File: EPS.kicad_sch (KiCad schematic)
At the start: 42 parts, among them SW101 Deploy, SW102 Deploy

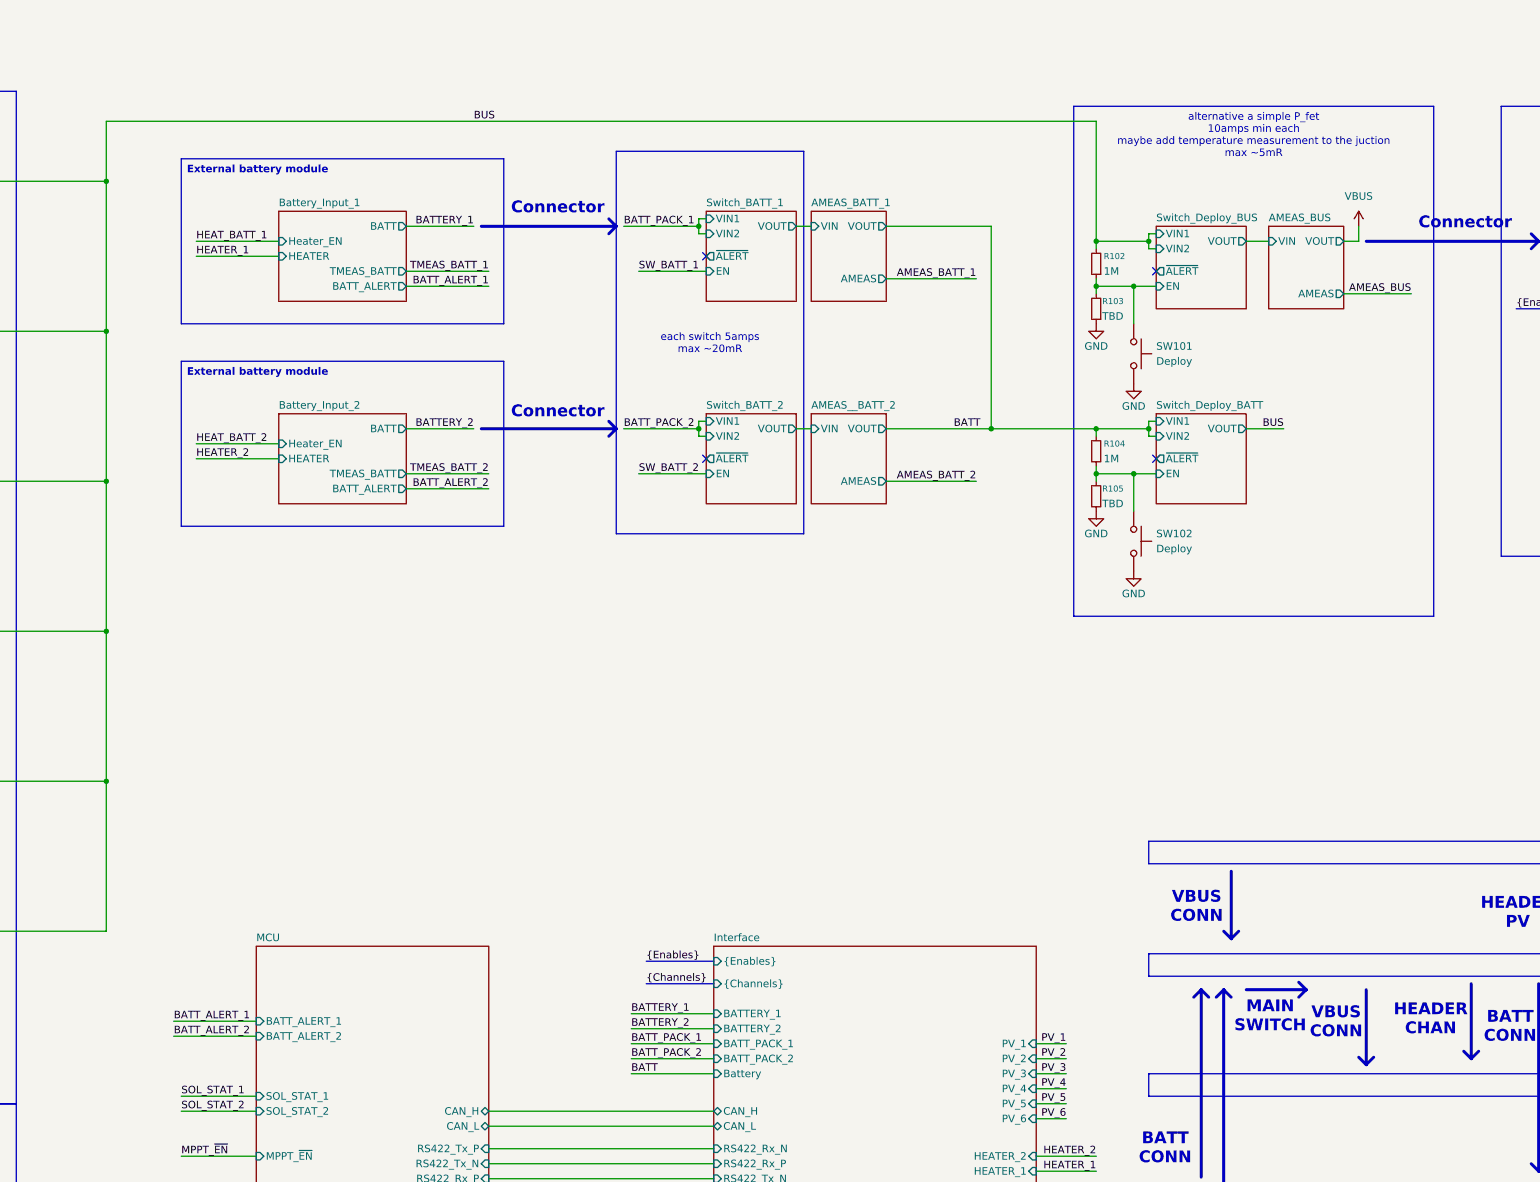
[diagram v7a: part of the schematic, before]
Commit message: deleted switch conncected to both batteries, modev pc104 connector to ti own sheet
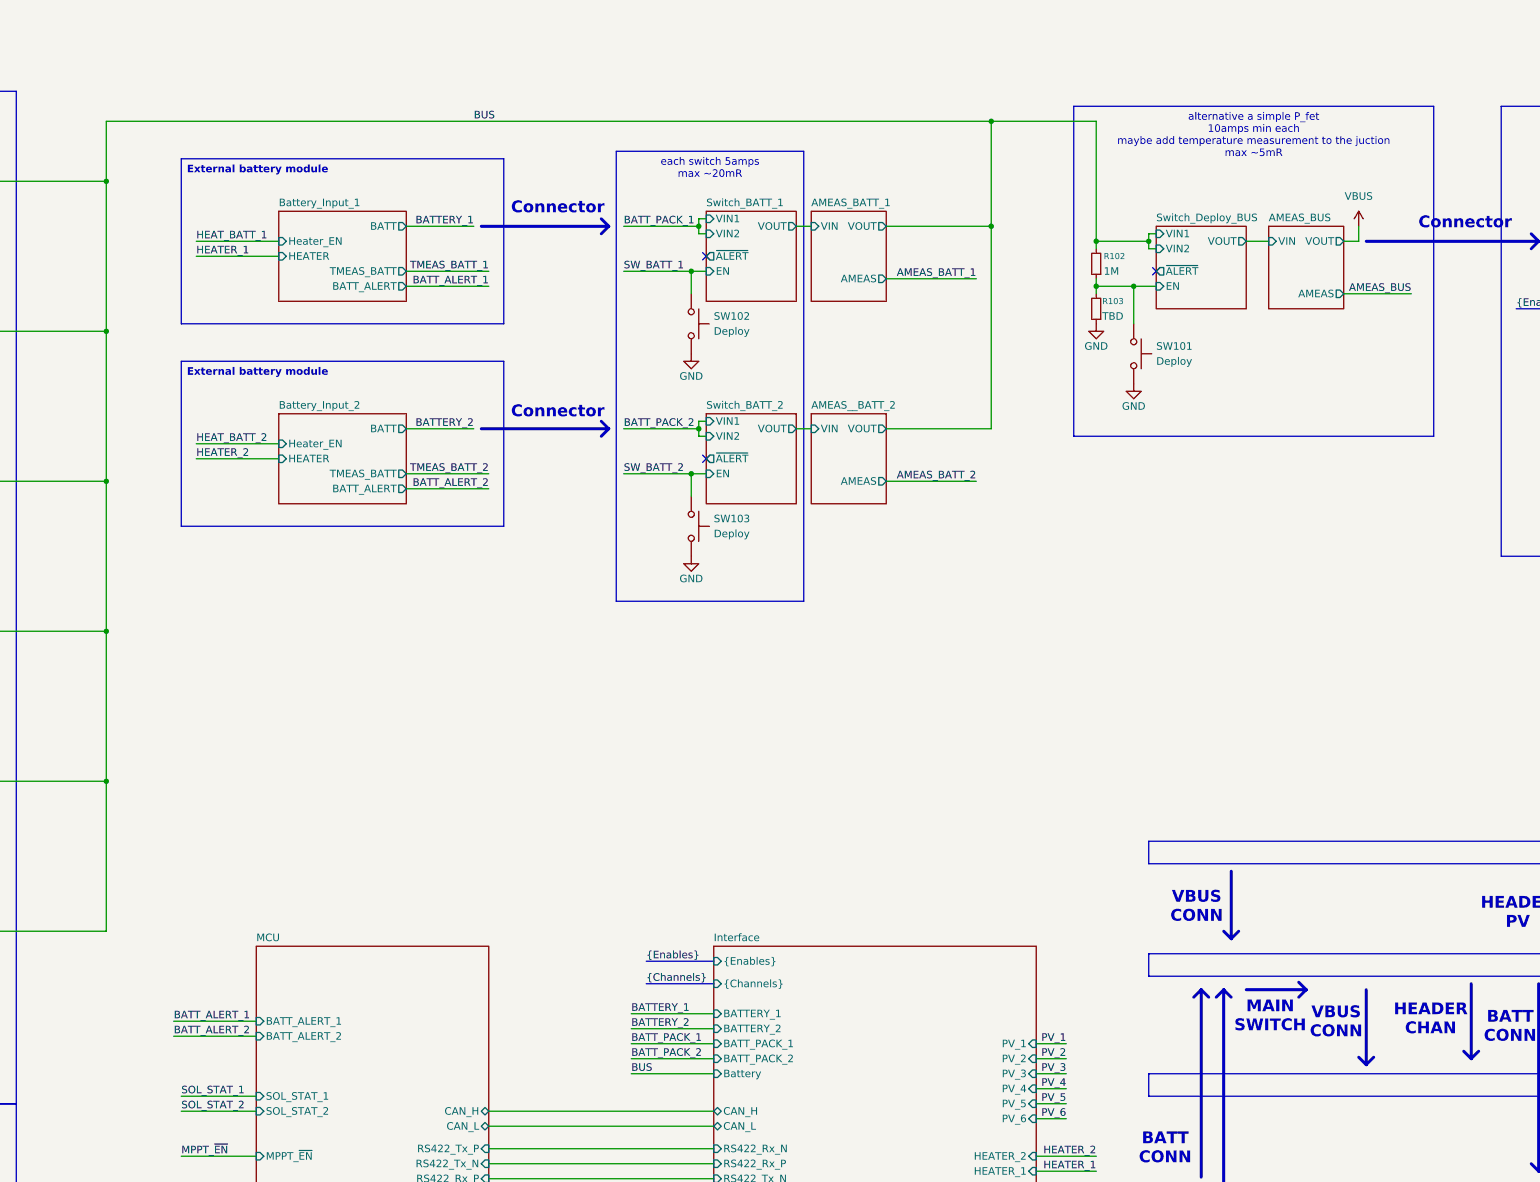
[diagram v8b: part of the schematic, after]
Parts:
- removed R104: 1M, Resistor_SMD:R_0603_1608Metric_Pad0.98x0.95mm_HandSolder, symbol Device:R_Small
- removed R105: TBD, Resistor_SMD:R_0603_1608Metric_Pad0.98x0.95mm_HandSolder, symbol Device:R_Small
- added SW103: Deploy, symbol Switch:SW_Push
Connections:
- net Switch_Deploy_BATT/EN is gone; now on net SW_BATT_1: SW102.1
- net GND: now also SW103.2
- net SW_BATT_2: now also SW103.1
- no-connect marks 4 -> 3
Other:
- removed sheet Switch_Deploy_BATT
- moved on the sheet: SW102
